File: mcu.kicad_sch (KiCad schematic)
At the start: 35 parts, among them CN1 HX JN1.27-2X5 TP H4.9, J1 DM3CS-SF, SW1 TS-1088-AR02016, U1 STM32F405RGTx, U6 SS12D10G5, X1 X1E000210127000G

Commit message: MCU connected
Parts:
- removed D5: BLUE LED, symbol Device:LED
- removed R12: 330, symbol Device:R
- added C23, C24, C25, C26, C27: 100n, symbol Device:C
- added C28: 10u, symbol Device:C
- added C29: 10n, symbol Device:C
- added C30, C31: 1u, symbol Device:C
- added C32, C33: 2.2, symbol Device:C
- added L2: 10n, symbol Device:L
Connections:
- net +3.3V is gone; now on net +3V3: C1.2, C2.2, C3.2, C4.2, C5.2, C6.2, C7.2, C8.2, CN1.1, CN1.3, CN1.5, CN1.9, D2.1 (K), D3.1 (K), D4.1 (K), ER-OLEDM015-2W.1 (GND), J1.6 (VSS), J1.S1 (GND), J1.S2 (GND), J1.S3 (GND), J1.S5 (GND), R8.2, SW1.2, U6.1, X1.2 (GND), X1.4 (GND)
- net NRST is gone; now on net MCU_NRST: CN1.10
- net +3V3: now also U1.1 (VBAT), U1.12 (VSSA), U1.18 (VSS), U1.19 (VDD), U1.32 (VDD), U1.48 (VDD), U1.63 (VSS), U1.64 (VDD), C23.1, C23.2, C24.1, C24.2, C25.1, C25.2, C26.1, C26.2, C27.1, C27.2, C28.1, C28.2, C29.2, C30.2, C31.1, C31.2, C32.2, C33.2, L2.2
- net HSE_IN: no longer U1.5 (PH0)
- net HSE_OUT: no longer U1.6 (PH1)
- net LED_0: now also U1.43 (PA10)
- net LED_1: now also U1.42 (PA9)
- net LED_2: now also U1.41 (PA8)
- net MCU_BOOT0: no longer U1.60 (BOOT0)
- net MCU_SDIO_CK: now also U1.53 (PC12)
- net MCU_SDIO_CMD: now also U1.54 (PD2)
- net MCU_SDIO_D0: now also U1.39 (PC8)
- net MCU_SDIO_D1: now also U1.40 (PC9)
- net MCU_SDIO_D2: now also U1.51 (PC10)
- net MCU_SDIO_D3: now also U1.52 (PC11)
- net SD_CARD_DETECT: now also U1.50 (PA15)
- net SWDCLK: now also U1.49 (PA14)
- net SWDIO: now also U1.46 (PA13)
- net SWO: now also U1.55 (PB3)
- net at U1.13 (VDDA): now also C29.1, C30.1, L2.1
- net POT_MUX_ADC: now reaches U1.14 (PA0)
- net POT_MUX_SEL_2: now reaches U1.26 (PB0)
- net POT_MUX_SEL_1: now reaches U1.27 (PB1)
- net POT_MUX_SEL_0: now reaches U1.28 (PB2)
- net at U1.31 (VCAP_1): now also C33.1
- net MCU_USB_D-: now reaches U1.44 (PA11)
- net MCU_USB_D+: now reaches U1.45 (PA12)
- net at U1.47 (VCAP_2): now also C32.1
- new net MCU_HSE_IN: U1.5 (PH0)
- new net MCU_HSE_OUT: U1.6 (PH1)
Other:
- note added: "MCU_VCAP_1"
- note added: "MCU_VCAP_2"
- moved on the sheet: C1, C2, C3, C4, C5, C6, CN1, D2, D3, D4, ER-OLEDM015-2W, FB1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

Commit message: adding anotations
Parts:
- renumbered C7 to C34, C8 to C35, C3 to C36, C4 to C37, C1 to C38, C5 to C39, C2 to C40, C6 to C41, D1 to D5, ER-OLEDM015-2W to ER-OLEDM015-2W1, FB1 to FB2, J1 to J5, R8 to R11, R1 to R12, R9 to R16, R10 to R17, R7 to R18, R2 to R19, R3 to R20, R4 to R21, R5 to R22, R6 to R23, SW1 to SW3
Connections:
- net HSE_IN is gone; now on net MCU_HSE_IN: C34.1, X1.1 (OSC1)
- net HSE_OUT is gone; now on net MCU_HSE_OUT: R17.2
- net MCU_BOOT0: now also U1.60 (BOOT0)
- no-connect marks 1 -> 20

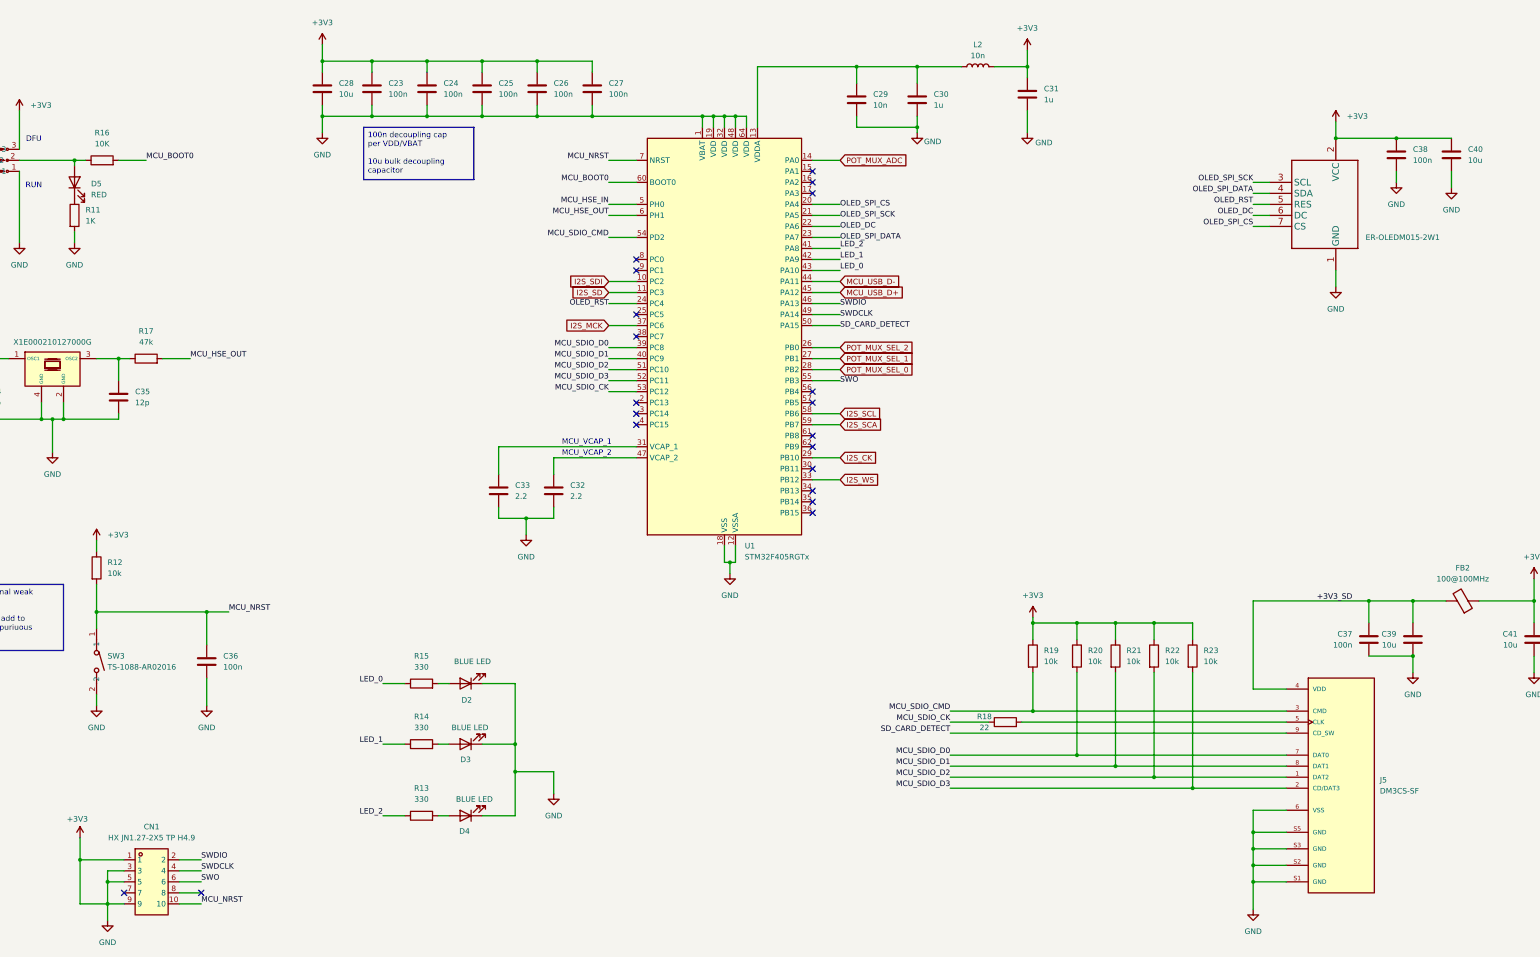
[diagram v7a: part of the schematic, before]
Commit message: ERC fixed
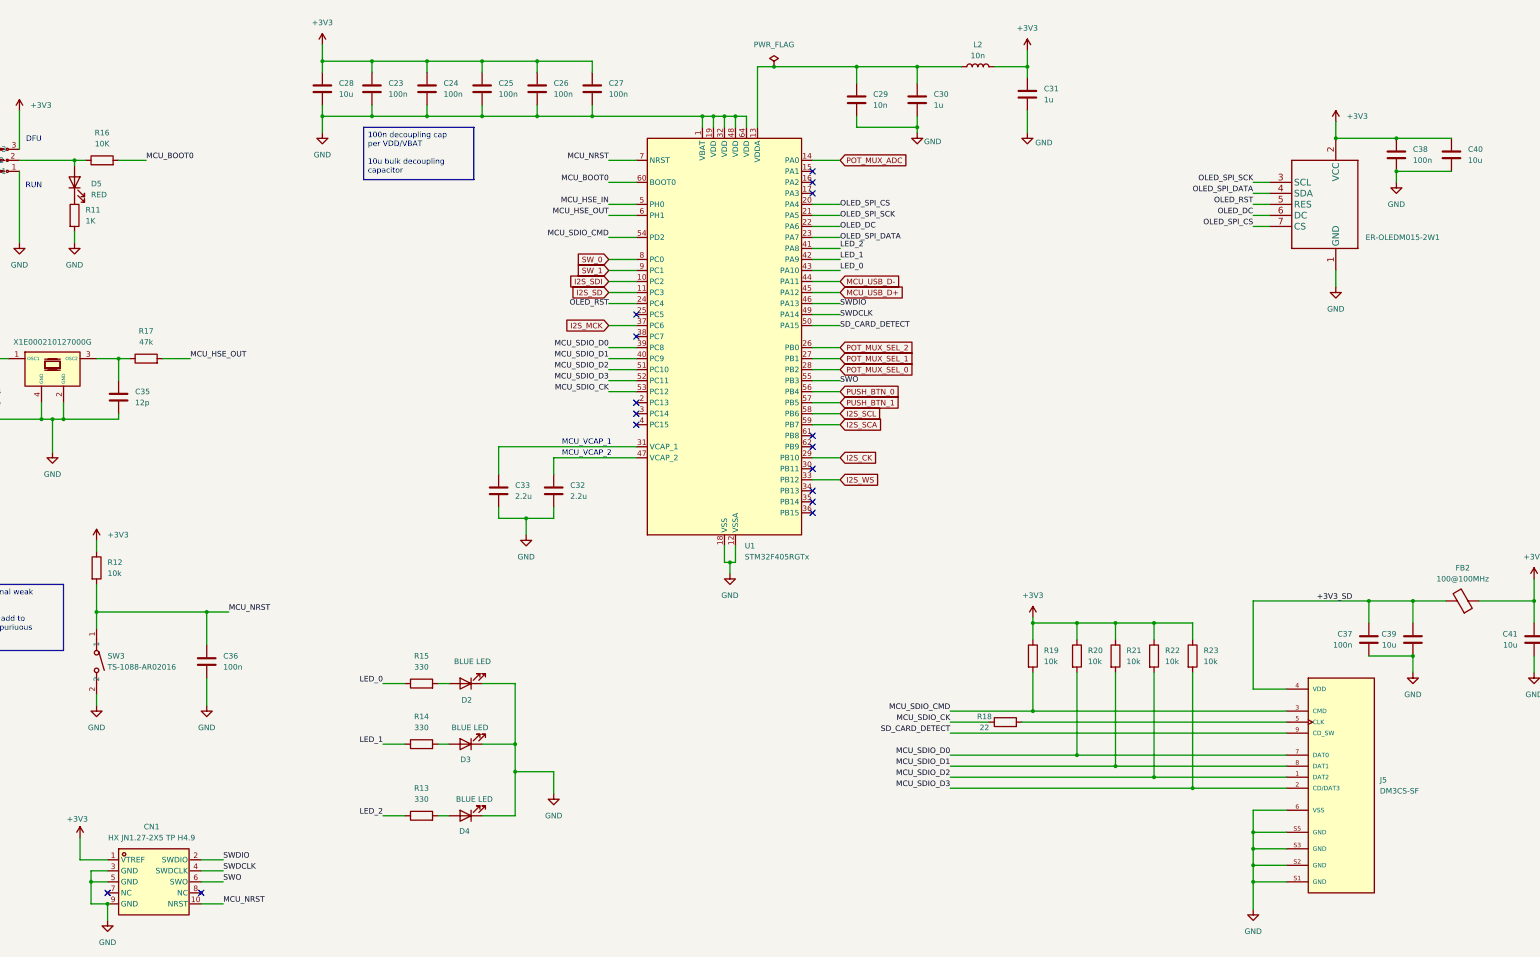
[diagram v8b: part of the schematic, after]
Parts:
- C32, C33: value 2.2 -> 2.2u
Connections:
- net +3V3: no longer C23.2, C24.2, C25.2, C26.2, C27.2, C28.2, C29.2, C30.2, C31.2, C32.2, C33.2, C34.2, C35.2, C36.2, C37.2, C38.2, C39.2, C40.2, C41.2, CN1.3, CN1.5, CN1.9, D2.1 (K), D3.1 (K), D4.1 (K), ER-OLEDM015-2W1.1 (GND), J5.6 (VSS), J5.S1 (GND), J5.S2 (GND), J5.S3 (GND), J5.S5 (GND), R11.2, SW3.2, U1.1 (VBAT), U1.12 (VSSA), U1.18 (VSS), U1.19 (VDD), U1.32 (VDD), U1.48 (VDD), U1.63 (VSS), U1.64 (VDD), U6.1, X1.2 (GND), X1.4 (GND)
- net PUSH_BTN_0: now reaches U1.56 (PB4)
- net PUSH_BTN_1: now reaches U1.57 (PB5)
- net SW_0: now reaches U1.8 (PC0)
- net SW_1: now reaches U1.9 (PC1)
- new net GND: C23.2, C24.2, C25.2, C26.2, C27.2, C28.2, C29.2, C30.2, C31.2, C32.2, C33.2, C34.2, C35.2, C36.2, C37.2, C38.2, C39.2, C40.2, C41.2, CN1.3 (GND), CN1.5 (GND), CN1.9 (GND), D2.1 (K), D3.1 (K), D4.1 (K), ER-OLEDM015-2W1.1 (GND), J5.6 (VSS), J5.S1 (GND), J5.S2 (GND), J5.S3 (GND), J5.S5 (GND), R11.2, SW3.2, U1.1 (VBAT), U1.12 (VSSA), U1.18 (VSS), U1.19 (VDD), U1.32 (VDD), U1.48 (VDD), U1.63 (VSS), U1.64 (VDD), U6.1, X1.2 (GND), X1.4 (GND)
- no-connect marks 20 -> 16
